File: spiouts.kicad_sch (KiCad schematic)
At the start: 4 parts, among them J12 Conn_01x07_MountingPin, J13 Conn_01x07_MountingPin, J14 Conn_01x07_MountingPin, J4 Conn_01x07_MountingPin

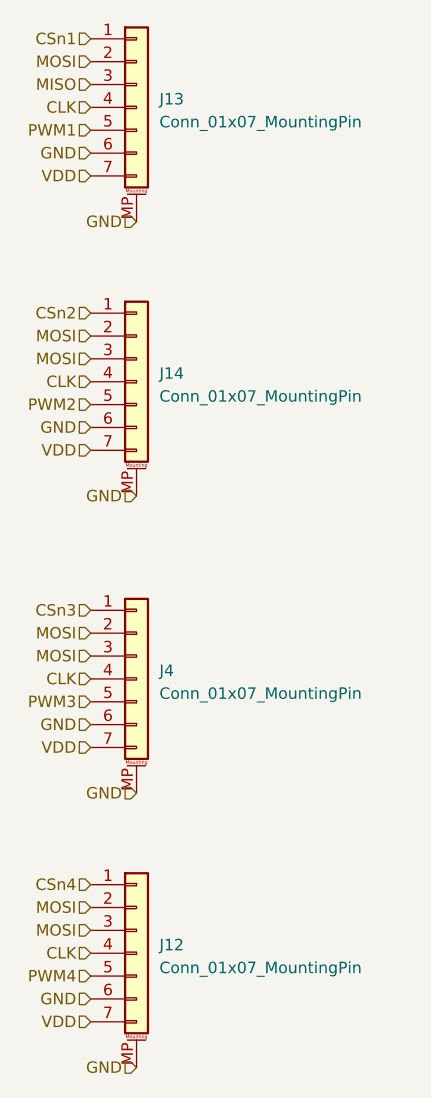
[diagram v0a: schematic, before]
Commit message: silkscreen changes, start routing spi
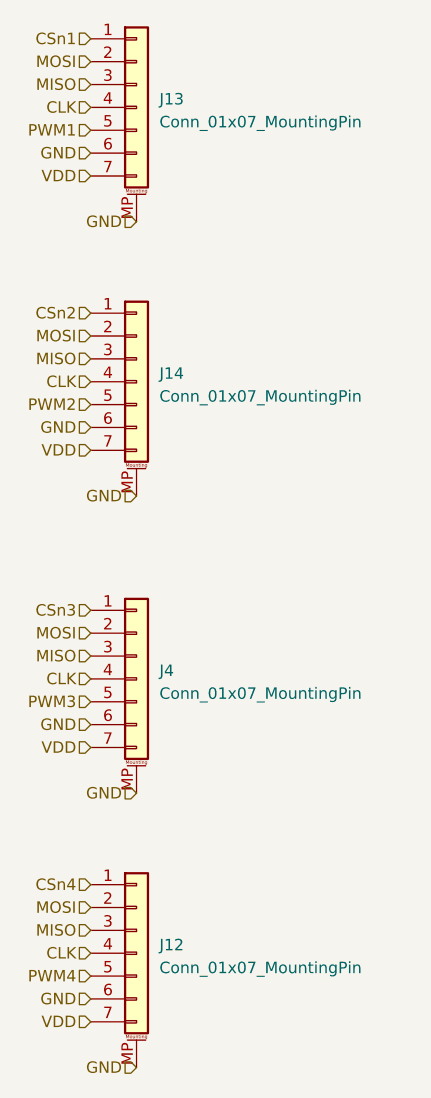
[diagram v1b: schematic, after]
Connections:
- net MISO: now also J12.3 (Pin_3), J14.3 (Pin_3), J4.3 (Pin_3)
- net MOSI: no longer J12.3 (Pin_3), J14.3 (Pin_3), J4.3 (Pin_3)
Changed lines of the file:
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@@
+		)
+	)
+	(hierarchical_label "CSn1"
+		(shape input)
+		(at 73.66 29.21 180)
+		(fields_autoplaced yes)
+		(effects
+			(font
+				(size 1.27 1.27)
+			)
+			(justify right)
+		)
+	)
+	(hierarchical_label "MISO"
+		(shape input)
+		(at 73.66 64.77 180)
+		(fields_autoplaced yes)
+		(effects
+			(font
+				(size 1.27 1.27)
+			)
+			(justify right)
+		)
+	)
+	(hierarchical_label "CSn4"
+		(shape input)
+		(at 73.66 123.19 180)
+		(fields_autoplaced yes)
+		(effects
+			(font
+				(size 1.27 1.27)
+			)
+			(justify right)
+		)
+	)
+	(hierarchical_label "GND"
+		(shape input)
+		(at 73.66 72.39 180)
+		(fields_autoplaced yes)
+		(effects
+			(font
+				(size 1.27 1.27)
+			)
+			(justify right)
+		)
+	)
+	(hierarchical_label "CLK"
+		(shape input)
+		(at 73.66 67.31 180)
+		(fields_autoplaced yes)
+		(effects
+			(font
+				(size 1.27 1.27)
+			)
+			(justify right)
+		)
+	)
+	(hierarchical_label "VDD"
+		(shape input)
+		(at 73.66 107.95 180)
+		(fields_autoplaced yes)
+		(effects
+			(font
+				(size 1.27 1.27)
+			)
+			(justify right)
+		)
+	)
+	(hierarchical_label "PWM3"
+		(shape input)
+		(at 73.66 102.87 180)
+		(fields_autoplaced yes)
+		(effects
+			(font
+				(size 1.27 1.27)
+			)
+			(justify right)
+		)
+	)
+	(hierarchical_label "CLK"
+		(shape input)
+		(at 73.66 36.83 180)
+		(fields_autoplaced yes)
+		(effects
+			(font
+				(size 1.27 1.27)
+			)
+			(justify right)
+		)
+	)
+	(hierarchical_label "GND"
+		(shape input)
+		(at 73.66 135.89 180)
+		(fields_autoplaced yes)
+		(effects
+			(font
+				(size 1.27 1.27)
+			)
+			(justify right)
+		)
+	)
+	(hierarchical_label "MISO"
+		(shape input)
+		(at 73.66 34.29 180)
+		(fields_autoplaced yes)
+		(effects
+			(font
+				(size 1.27 1.27)
+			)
+			(justify right)
 		)
 	)
 	(hierarchical_label "MOSI"
 		(shape input)
+		(at 73.66 62.23 180)
+		(fields_autoplaced yes)
+		(effects
+			(font
+				(size 1.27 1.27)
+			)
+			(justify right)
+		)
+	)
+	(hierarchical_label "MOSI"
+		(shape input)
+		(at 73.66 125.73 180)
+		(fields_autoplaced yes)
+		(effects
+			(font
+				(size 1.27 1.27)
+			)
+			(justify right)
+		)
+	)
+	(hierarchical_label "MISO"
+		(shape input)
 		(at 73.66 97.79 180)
 		(fields_autoplaced yes)
@@
 		)
 	)
-	(hierarchical_label "CSn1"
-		(shape input)
-		(at 73.66 29.21 180)
-		(fields_autoplaced yes)
-		(effects
-			(font
-				(size 1.27 1.27)
-			)
-			(justify right)
-		)
-	)
-	(hierarchical_label "CSn4"
-		(shape input)
-		(at 73.66 123.19 180)
-		(fields_autoplaced yes)
-		(effects
-			(font
-				(size 1.27 1.27)
-			)
-			(justify right)
-		)
-	)
-	(hierarchical_label "GND"
-		(shape input)
-		(at 73.66 72.39 180)
+	(hierarchical_label "GND"
+		(shape input)
+		(at 78.74 143.51 180)
+		(fields_autoplaced yes)
+		(effects
+			(font
+				(size 1.27 1.27)
+			)
+			(justify right)
+		)
+	)
+	(hierarchical_label "PWM2"
+		(shape input)
+		(at 73.66 69.85 180)
+		(fields_autoplaced yes)
+		(effects
+			(font
+				(size 1.27 1.27)
+			)
+			(justify right)
+		)
+	)
+	(hierarchical_label "PWM4"
+		(shape input)
+		(at 73.66 133.35 180)
+		(fields_autoplaced yes)
+		(effects
+			(font
+				(size 1.27 1.27)
+			)
+			(justify right)
+		)
+	)
+	(hierarchical_label "PWM1"
+		(shape input)
+		(at 73.66 39.37 180)
+		(fields_autoplaced yes)
+		(effects
+			(font
+				(size 1.27 1.27)
+			)
+			(justify right)
+		)
+	)
+	(hierarchical_label "MOSI"
+		(shape input)
+		(at 73.66 31.75 180)
 		(fields_autoplaced yes)
 		(effects
@@
 	(hierarchical_label "CLK"
 		(shape input)
-		(at 73.66 67.31 180)
+		(at 73.66 100.33 180)
+		(fields_autoplaced yes)
+		(effects
+			(font
+				(size 1.27 1.27)
+			)
+			(justify right)
+		)
+	)
+	(hierarchical_label "GND"
+		(shape input)
+		(at 73.66 105.41 180)
+		(fields_autoplaced yes)
+		(effects
+			(font
+				(size 1.27 1.27)
+			)
+			(justify right)
+		)
+	)
+	(hierarchical_label "GND"
+		(shape input)
+		(at 78.74 80.01 180)
 		(fields_autoplaced yes)
 		(effects
@@
 	(hierarchical_label "VDD"
 		(shape input)
-		(at 73.66 107.95 180)
-		(fields_autoplaced yes)
-		(effects
-			(font
-				(size 1.27 1.27)
-			)
-			(justify right)
-		)
-	)
-	(hierarchical_label "PWM3"
-		(shape input)
-		(at 73.66 102.87 180)
-		(fields_autoplaced yes)
-		(effects
-			(font
-				(size 1.27 1.27)
-			)
-			(justify right)
-		)
-	)
-	(hierarchical_label "MOSI"
+		(at 73.66 138.43 180)
+		(fields_autoplaced yes)
+		(effects
+			(font
+				(size 1.27 1.27)
+			)
+			(justify right)
+		)
+	)
+	(hierarchical_label "CSn3"
+		(shape input)
+		(at 73.66 92.71 180)
+		(fields_autoplaced yes)
+		(effects
+			(font
+				(size 1.27 1.27)
+			)
+			(justify right)
+		)
+	)
+	(hierarchical_label "MISO"
 		(shape input)
 		(at 73.66 128.27 180)
 		(fields_autoplaced yes)
 		(effects
-			(font
-				(size 1.27 1.27)
-			)
-			(justify right)
-		)
-	)
-	(hierarchical_label "CLK"
-		(shape input)
-		(at 73.66 36.83 180)
-		(fields_autoplaced yes)
-		(effects
-			(font
-				(size 1.27 1.27)
-			)
-			(justify right)
-		)
-	)
-	(hierarchical_label "GND"
-		(shape input)
-		(at 73.66 135.89 180)
-		(fields_autoplaced yes)
-		(effects
-			(font
-				(size 1.27 1.27)
-			)
-			(justify right)
-		)
-	)
-	(hierarchical_label "MISO"
-		(shape input)
-		(at 73.66 34.29 180)
-		(fields_autoplaced yes)
-		(effects
-			(font
-				(size 1.27 1.27)
-			)
-			(justify right)
-		)
-	)
-	(hierarchical_label "MOSI"
-		(shape input)
-		(at 73.66 62.23 180)
-		(fields_autoplaced yes)
-		(effects
-			(font
-				(size 1.27 1.27)
-			)
-			(justify right)
-		)
-	)
-	(hierarchical_label "MOSI"
-		(shape input)
-		(at 73.66 125.73 180)
-		(fields_autoplaced yes)
-		(effects
-			(font
-				(size 1.27 1.27)
-			)
-			(justify right)
-		)
-	)
-	(hierarchical_label "GND"
-		(shape input)
-		(at 78.74 143.51 180)
-		(fields_autoplaced yes)
-		(effects
-			(font
-				(size 1.27 1.27)
-			)
-			(justify right)
-		)
-	)
-	(hierarchical_label "PWM2"
-		(shape input)
-		(at 73.66 69.85 180)
-		(fields_autoplaced yes)
-		(effects
-			(font
-				(size 1.27 1.27)
-			)
-			(justify right)
-		)
-	)
-	(hierarchical_label "PWM4"
-		(shape input)
-		(at 73.66 133.35 180)
-		(fields_autoplaced yes)
-		(effects
-			(font
-				(size 1.27 1.27)
-			)
-			(justify right)
-		)
-	)
-	(hierarchical_label "PWM1"
-		(shape input)
-		(at 73.66 39.37 180)
-		(fields_autoplaced yes)
-		(effects
-			(font
-				(size 1.27 1.27)
-			)
-			(justify right)
-		)
-	)
-	(hierarchical_label "MOSI"
-		(shape input)
-		(at 73.66 31.75 180)
-		(fields_autoplaced yes)
-		(effects
-			(font
-				(size 1.27 1.27)
-			)
-			(justify right)
-		)
-	)
-	(hierarchical_label "CLK"
-		(shape input)
-		(at 73.66 100.33 180)
-		(fields_autoplaced yes)
-		(effects
-			(font
-				(size 1.27 1.27)
-			)
-			(justify right)
-		)
-	)
-	(hierarchical_label "GND"
-		(shape input)
-		(at 73.66 105.41 180)
-		(fields_autoplaced yes)
-		(effects
-			(font
-				(size 1.27 1.27)
-			)
-			(justify right)
-		)
-	)
-	(hierarchical_label "GND"
-		(shape input)
-		(at 78.74 80.01 180)
-		(fields_autoplaced yes)
-		(effects
-			(font
-				(size 1.27 1.27)
-			)
-			(justify right)
-		)
-	)
-	(hierarchical_label "MOSI"
-		(shape input)
-		(at 73.66 64.77 180)
-		(fields_autoplaced yes)
-		(effects
-			(font
-				(size 1.27 1.27)
-			)
-			(justify right)
-		)
-	)
-	(hierarchical_label "VDD"
-		(shape input)
-		(at 73.66 138.43 180)
-		(fields_autoplaced yes)
-		(effects
-			(font
-				(size 1.27 1.27)
-			)
-			(justify right)
-		)
-	)
-	(hierarchical_label "CSn3"
-		(shape input)
-		(at 73.66 92.71 180)
-		(fields_autoplaced yes)
-		(effects
